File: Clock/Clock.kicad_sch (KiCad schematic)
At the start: 65 parts, among them J1 Conn buss, J10 Conn_buss, J11 Conn_buss, J12 Conn_buss, J13 Register_A-1,2 LED Conn, J14 Register_B-1,2 LED Conn, J15 Program Counter LED Conn, J16 Memory Address Reg LED Conn, J17 Instruction Reg LED Conn, J18 Conn_01x02_Pin, J19 Conn_02x04_Top_Bottom, J2 USB4125-GF-A, J3 Fuse-Block, J4 Conn buss, J5 Conn_buss, J6 Conn_buss, J7 Conn_buss, J8 Conn_buss, J9 Conn_buss, SW1 SW_CLK_mono, SW2 SW_Select_Mon/Ast, SW3 SW_SPST, SW4 SW_Select_Oscilator, U1 NE555P, U10 CD74HCT153E, U2 NE555P, U3 NE555P, U4 74LS04, U5 74LS08, U6 CD74HCT14E, U7 NE555P, U9 74HCT244, Y1 ECS-100AX-010

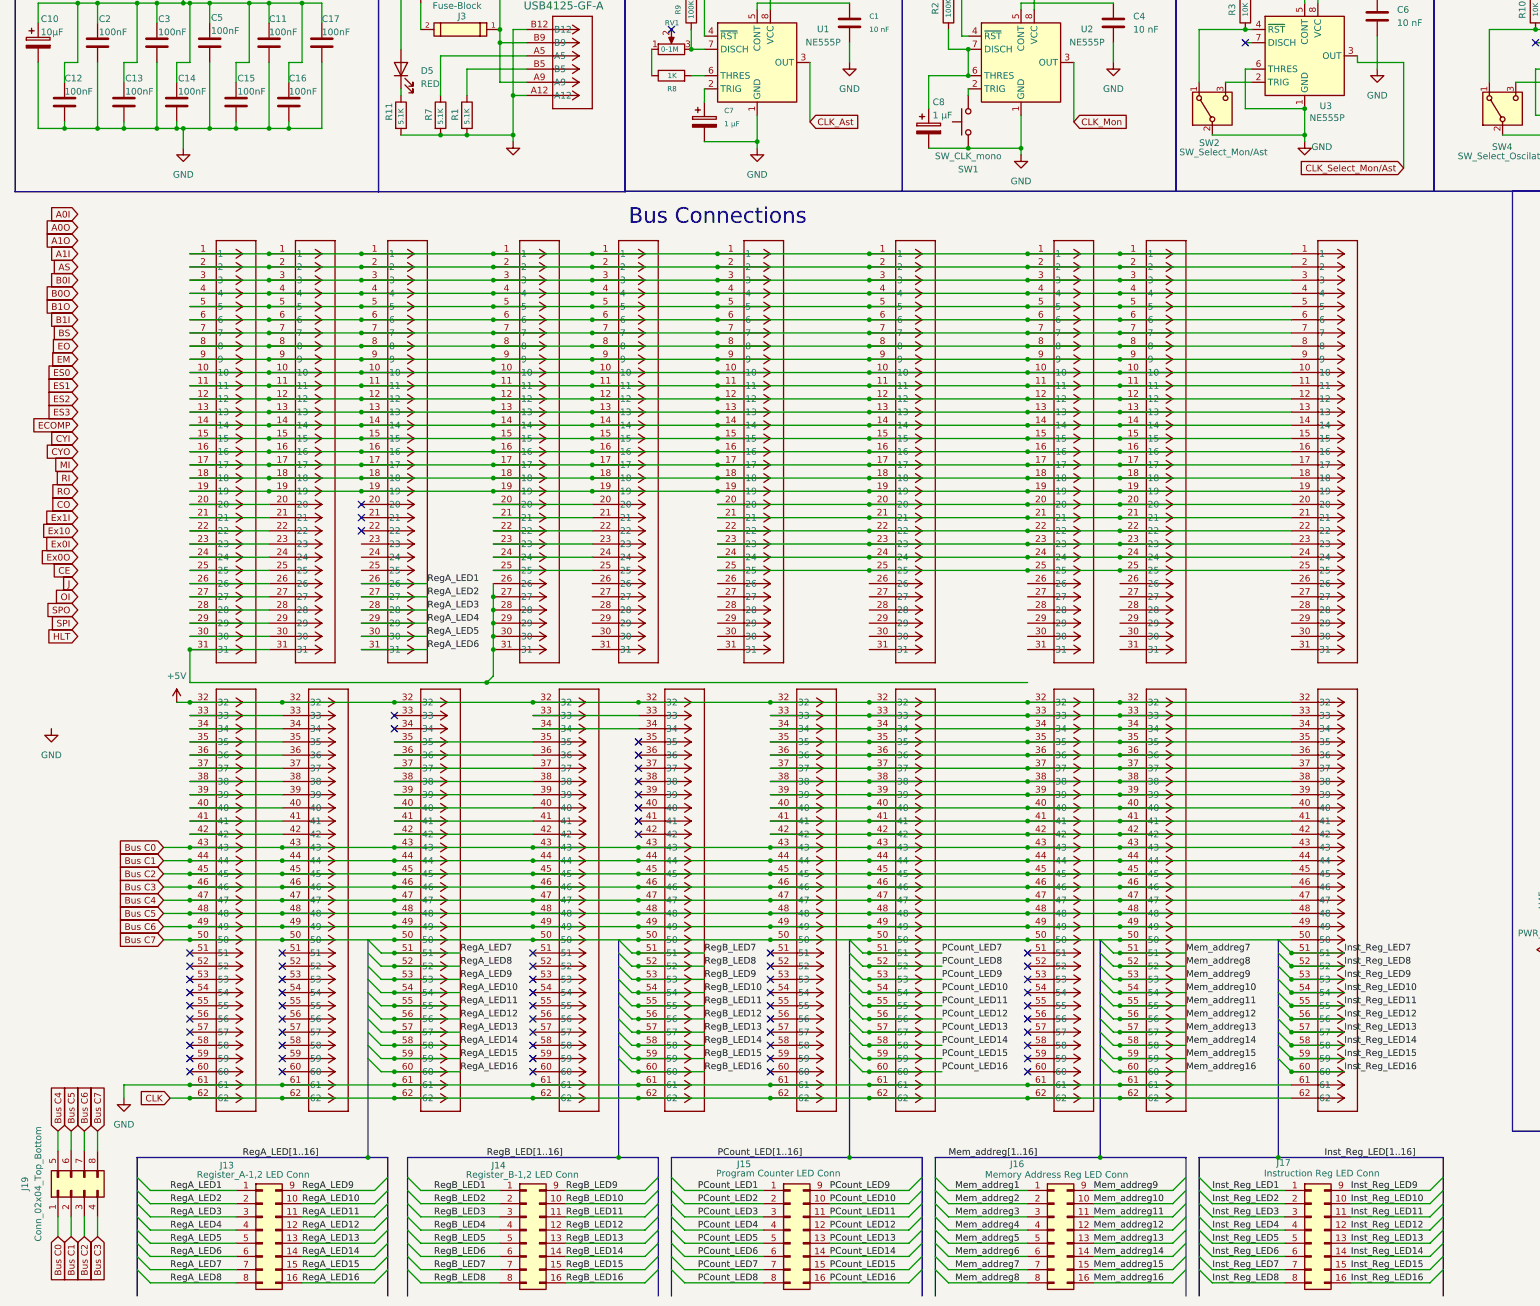
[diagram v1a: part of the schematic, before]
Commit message: Routed bus connector
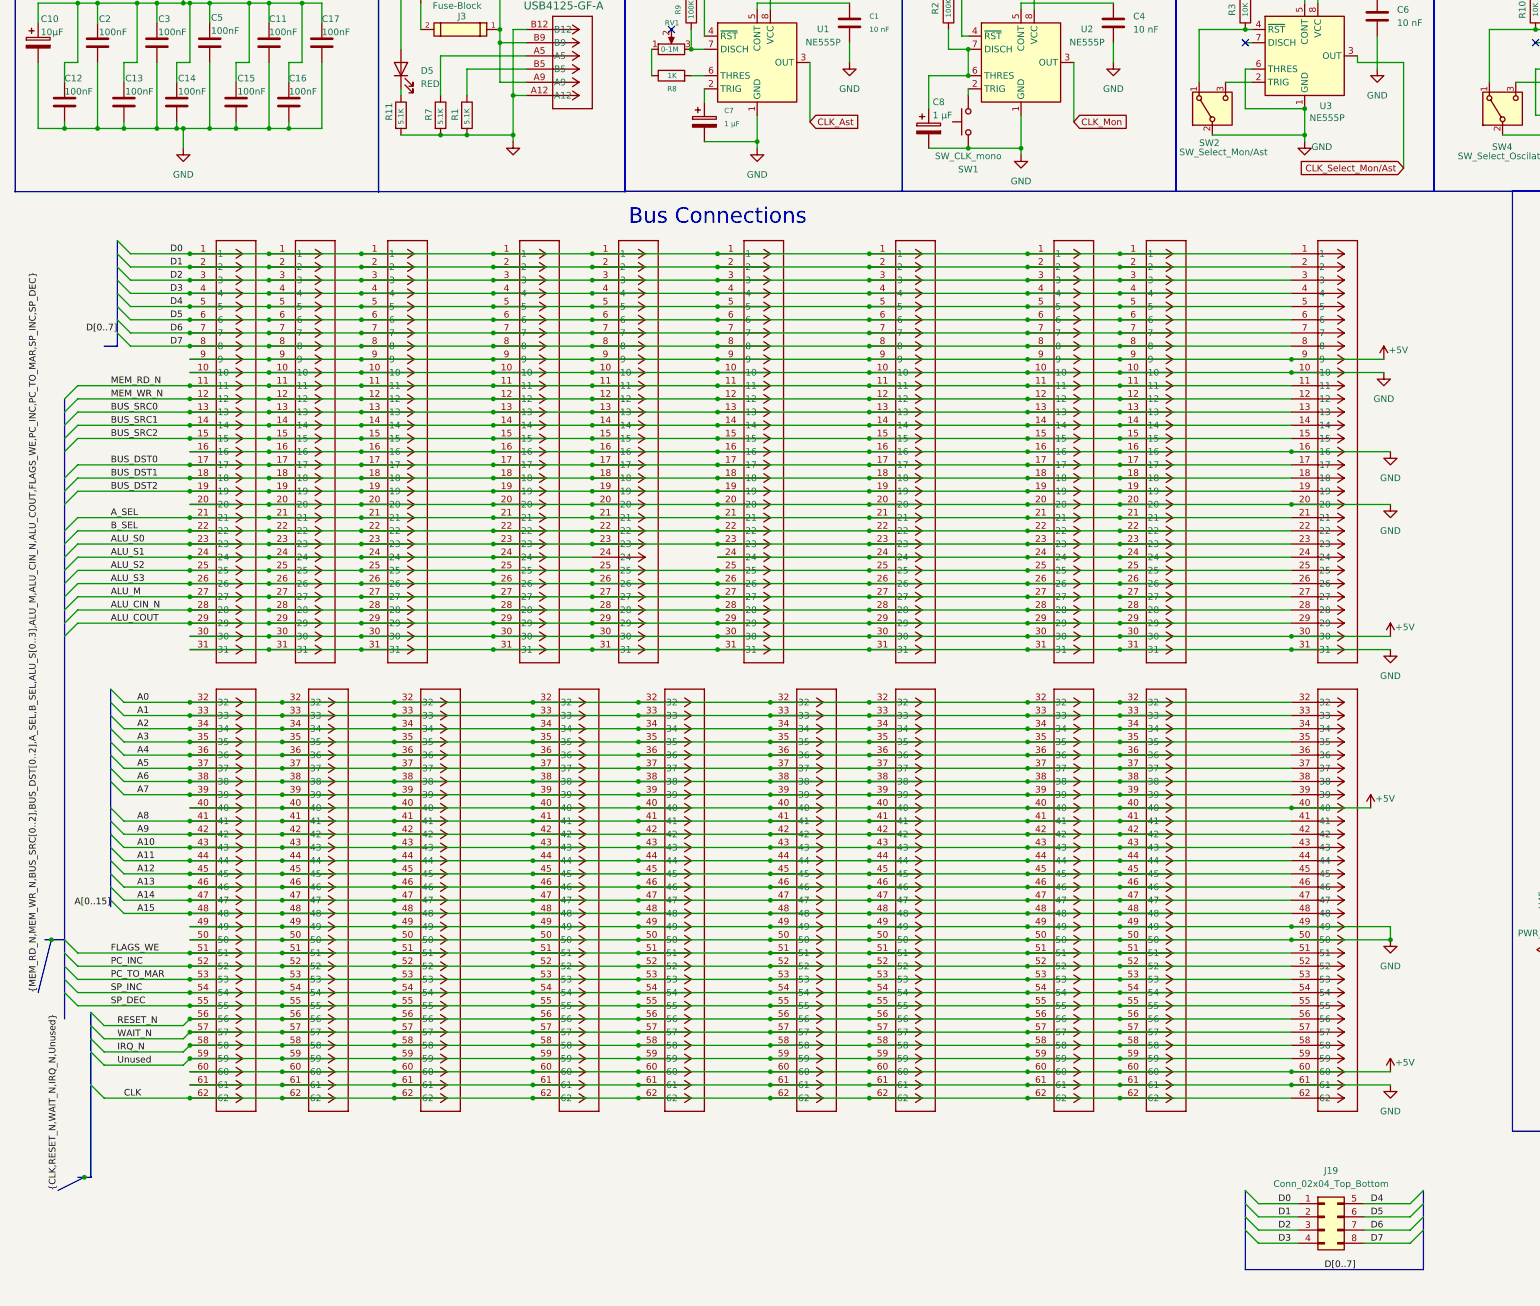
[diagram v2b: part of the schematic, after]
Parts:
- removed J13: Register_A-1,2 LED Conn, Connector_PinHeader_2.54mm:PinHeader_2x08_P2.54mm_Vertical, symbol Connector_Generic:Conn_02x08_Top_Bottom
- removed J14: Register_B-1,2 LED Conn, Connector_PinHeader_2.54mm:PinHeader_2x08_P2.54mm_Vertical, symbol Connector_Generic:Conn_02x08_Top_Bottom
- removed J15: Program Counter LED Conn, Connector_PinHeader_2.54mm:PinHeader_2x08_P2.54mm_Vertical, symbol Connector_Generic:Conn_02x08_Top_Bottom
- removed J16: Memory Address Reg LED Conn, Connector_PinHeader_2.54mm:PinHeader_2x08_P2.54mm_Vertical, symbol Connector_Generic:Conn_02x08_Top_Bottom
- removed J17: Instruction Reg LED Conn, Connector_PinHeader_2.54mm:PinHeader_2x08_P2.54mm_Vertical, symbol Connector_Generic:Conn_02x08_Top_Bottom
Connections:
- net Inst_Reg_LED10 is gone; now on net SP_INC: J1.54
- net Inst_Reg_LED11 is gone; now on net SP_DEC: J1.55
- net Inst_Reg_LED12 is gone; now on net RESET_N: J1.56
- net Inst_Reg_LED13 is gone; now on net WAIT_N: J1.57
- net Inst_Reg_LED14 is gone; now on net IRQ_N: J1.58
- net Inst_Reg_LED15 is gone; now on net Unused: J1.59
- net Inst_Reg_LED16 is gone; now on net +5V: J1.60
- net Inst_Reg_LED7 is gone; now on net FLAGS_WE: J1.51
- net Inst_Reg_LED8 is gone; now on net PC_INC: J1.52
- net Inst_Reg_LED9 is gone; now on net PC_TO_MAR: J1.53
- net Mem_addreg10 is gone; now on net SP_INC: J5.54
- net Mem_addreg11 is gone; now on net SP_DEC: J5.55
- net Mem_addreg12 is gone; now on net RESET_N: J5.56
- net Mem_addreg13 is gone; now on net WAIT_N: J5.57
- net Mem_addreg14 is gone; now on net IRQ_N: J5.58
- net Mem_addreg15 is gone; now on net Unused: J5.59
- net Mem_addreg16 is gone; now on net +5V: J5.60
- net Mem_addreg7 is gone; now on net FLAGS_WE: J5.51
- net Mem_addreg8 is gone; now on net PC_INC: J5.52
- net Mem_addreg9 is gone; now on net PC_TO_MAR: J5.53
- net PCount_LED10 is gone; now on net SP_INC: J8.54
- net PCount_LED11 is gone; now on net SP_DEC: J8.55
- net PCount_LED12 is gone; now on net RESET_N: J8.56
- net PCount_LED13 is gone; now on net WAIT_N: J8.57
- net PCount_LED14 is gone; now on net IRQ_N: J8.58
- net PCount_LED15 is gone; now on net Unused: J8.59
- net PCount_LED16 is gone; now on net +5V: J8.60
- net PCount_LED7 is gone; now on net FLAGS_WE: J8.51
- net PCount_LED8 is gone; now on net PC_INC: J8.52
- net PCount_LED9 is gone; now on net PC_TO_MAR: J8.53
- net RegA_LED1 is gone; now on net ALU_S3: J11.26
- net RegA_LED10 is gone; now on net SP_INC: J11.54
- net RegA_LED11 is gone; now on net SP_DEC: J11.55
- net RegA_LED12 is gone; now on net RESET_N: J11.56
- net RegA_LED13 is gone; now on net WAIT_N: J11.57
- net RegA_LED14 is gone; now on net IRQ_N: J11.58
- net RegA_LED15 is gone; now on net Unused: J11.59
- net RegA_LED16 is gone; now on net +5V: J11.60
- net RegA_LED2 is gone; now on net ALU_M: J11.27
- net RegA_LED3 is gone; now on net ALU_CIN_N: J11.28
- net RegA_LED4 is gone; now on net ALU_COUT: J11.29
- net RegA_LED5 is gone; now on net +5V: J11.30
- net RegA_LED6 is gone; now on net GND: J11.31
- net RegA_LED7 is gone; now on net FLAGS_WE: J11.51
- net RegA_LED8 is gone; now on net PC_INC: J11.52
- net RegA_LED9 is gone; now on net PC_TO_MAR: J11.53
- net RegB_LED10 is gone; now on net SP_INC: J9.54
- net RegB_LED11 is gone; now on net SP_DEC: J9.55
- net RegB_LED12 is gone; now on net RESET_N: J9.56
- net RegB_LED13 is gone; now on net WAIT_N: J9.57
- net RegB_LED14 is gone; now on net IRQ_N: J9.58
- net RegB_LED15 is gone; now on net Unused: J9.59
- net RegB_LED16 is gone; now on net +5V: J9.60
- net RegB_LED7 is gone; now on net FLAGS_WE: J9.51
- net RegB_LED8 is gone; now on net PC_INC: J9.52
- net RegB_LED9 is gone; now on net PC_TO_MAR: J9.53
- net +5V: now also J1.30, J1.40, J1.9, J10.30, J10.40, J10.60, J10.9, J11.40, J11.9, J12.30, J12.40, J12.60, J12.9, J4.30, J4.40, J4.60, J4.9, J5.30, J5.40, J5.9, J6.30, J6.40, J6.60, J6.9, J7.30, J7.40, J7.60, J7.9, J8.30, J8.40, J8.9, J9.30, J9.40, J9.9; no longer J1.32, J10.32, J11.32, J12.32, J4.32, J5.32, J6.32, J7.32, J8.32, J9.32
- net GND: now also J1.10, J1.16, J1.20, J1.31, J1.49, J1.50, J10.10, J10.16, J10.20, J10.31, J10.49, J10.50, J11.10, J11.16, J11.20, J11.49, J11.50, J12.10, J12.16, J12.20, J12.31, J12.49, J12.50, J4.10, J4.16, J4.20, J4.31, J4.49, J4.50, J5.10, J5.16, J5.20, J5.31, J5.49, J5.50, J6.10, J6.16, J6.20, J6.31, J6.49, J6.50, J7.10, J7.16, J7.20, J7.31, J7.49, J7.50, J8.10, J8.16, J8.20, J8.31, J8.49, J8.50, J9.10, J9.16, J9.20, J9.31, J9.49, J9.50
- net D0: now reaches J1.1, J10.1, J11.1, J12.1, J4.1, J5.1, J6.1, J7.1, J8.1, J9.1
- net D0: now also J19.1 (Pin_1)
- net MEM_RD_N: now reaches J1.11, J10.11, J11.11, J12.11, J4.11, J5.11, J6.11, J7.11, J8.11, J9.11
- net MEM_WR_N: now reaches J1.12, J10.12, J11.12, J12.12, J4.12, J5.12, J6.12, J7.12, J8.12, J9.12
- net BUS_SRC0: now reaches J1.13, J10.13, J11.13, J12.13, J4.13, J5.13, J6.13, J7.13, J8.13, J9.13
- net BUS_SRC1: now reaches J1.14, J10.14, J11.14, J12.14, J4.14, J5.14, J6.14, J7.14, J8.14, J9.14
- net BUS_SRC2: now reaches J1.15, J10.15, J11.15, J12.15, J4.15, J5.15, J6.15, J7.15, J8.15, J9.15
- net BUS_DST0: now reaches J1.17, J10.17, J11.17, J12.17, J4.17, J5.17, J6.17, J7.17, J8.17, J9.17
- net BUS_DST1: now reaches J1.18, J10.18, J11.18, J12.18, J4.18, J5.18, J6.18, J7.18, J8.18, J9.18
- net BUS_DST2: now reaches J1.19, J10.19, J11.19, J12.19, J4.19, J5.19, J6.19, J7.19, J8.19, J9.19
- net D1: now reaches J1.2, J10.2, J11.2, J12.2, J4.2, J5.2, J6.2, J7.2, J8.2, J9.2
- net D1: now also J19.2 (Pin_2)
- net A_SEL: now reaches J7.21, J9.21
- net A_SEL: now also J1.21, J10.21, J11.21, J12.21, J4.21, J5.21, J6.21, J8.21
- net B_SEL: now reaches J7.22, J9.22
- net B_SEL: now also J1.22, J10.22, J11.22, J12.22, J4.22, J5.22, J6.22, J8.22
- net ALU_S0: now reaches J7.23, J9.23
- net ALU_S0: now also J1.23, J10.23, J11.23, J12.23, J4.23, J5.23, J6.23, J8.23
- net ALU_S1: now reaches J7.24, J9.24
- net ALU_S1: now also J10.24, J11.24, J12.24
- net ALU_S2: now reaches J7.25, J9.25
- net ALU_S2: now also J1.25, J10.25, J11.25, J12.25, J4.25, J5.25, J6.25, J8.25
- net D2: now reaches J1.3, J10.3, J11.3, J12.3, J4.3, J5.3, J6.3, J7.3, J8.3, J9.3
- net D2: now also J19.3 (Pin_3)
- net D3: now reaches J1.4, J10.4, J11.4, J12.4, J4.4, J5.4, J6.4, J7.4, J8.4, J9.4
- net D3: now also J19.4 (Pin_4)
- net D4: now reaches J1.5, J10.5, J11.5, J12.5, J4.5, J5.5, J6.5, J7.5, J8.5, J9.5
- net D4: now also J19.5 (Pin_5)
- net D5: now reaches J1.6, J10.6, J11.6, J12.6, J4.6, J5.6, J6.6, J7.6, J8.6, J9.6
- net D5: now also J19.6 (Pin_6)
- net D6: now reaches J1.7, J10.7, J11.7, J12.7, J4.7, J5.7, J6.7, J7.7, J8.7, J9.7
- net D6: now also J19.7 (Pin_7)
- net D7: now reaches J1.8, J10.8, J11.8, J12.8, J4.8, J5.8, J6.8, J7.8, J8.8, J9.8
- net D7: now also J19.8 (Pin_8)
- net ALU_S3: now reaches J10.26, J12.26
- net ALU_S3: now also J1.26, J4.26, J5.26, J6.26, J7.26, J8.26, J9.26
- net ALU_M: now reaches J10.27, J12.27
- net ALU_M: now also J1.27, J4.27, J5.27, J6.27, J7.27, J8.27, J9.27
- net ALU_CIN_N: now reaches J10.28, J12.28
- net ALU_CIN_N: now also J1.28, J4.28, J5.28, J6.28, J7.28, J8.28, J9.28
- net ALU_COUT: now reaches J10.29, J12.29
- net ALU_COUT: now also J1.29, J4.29, J5.29, J6.29, J7.29, J8.29, J9.29
- net A1: now reaches J1.33, J4.33, J5.33, J6.33, J8.33
- net A1: now also J10.33, J11.33, J12.33, J7.33, J9.33
- net A2: now reaches J1.34, J4.34, J5.34, J6.34, J8.34
- net A2: now also J10.34, J11.34, J12.34, J7.34, J9.34
- net A3: now reaches J1.35, J4.35, J5.35, J6.35, J8.35
- net A3: now also J10.35, J11.35, J12.35, J7.35, J9.35
- net A4: now reaches J1.36, J4.36, J5.36, J6.36, J8.36
- net A4: now also J10.36, J11.36, J12.36, J7.36, J9.36
- net A5: now reaches J1.37, J4.37, J5.37, J6.37, J8.37
- net A5: now also J10.37, J11.37, J12.37, J7.37, J9.37
- net A6: now reaches J1.38, J4.38, J5.38, J6.38, J8.38
- net A6: now also J10.38, J11.38, J12.38, J7.38, J9.38
- net A7: now reaches J1.39, J4.39, J5.39, J6.39, J8.39
- net A7: now also J10.39, J11.39, J12.39, J7.39, J9.39
- net A8: now reaches J1.41, J4.41, J5.41, J6.41, J8.41
- net A8: now also J10.41, J11.41, J12.41, J7.41, J9.41
- net A9: now reaches J1.42, J4.42, J5.42, J6.42, J8.42
- net A9: now also J10.42, J11.42, J12.42, J7.42, J9.42
- net FLAGS_WE: now reaches J4.51
- net FLAGS_WE: now also J10.51, J12.51, J6.51, J7.51
- net PC_INC: now reaches J4.52
- net PC_INC: now also J10.52, J12.52, J6.52, J7.52
- net PC_TO_MAR: now reaches J4.53
- net PC_TO_MAR: now also J10.53, J12.53, J6.53, J7.53
- net SP_INC: now reaches J4.54
- net SP_INC: now also J10.54, J12.54, J6.54, J7.54
- net SP_DEC: now reaches J4.55
- net SP_DEC: now also J10.55, J12.55, J6.55, J7.55
- net RESET_N: now reaches J4.56
- net RESET_N: now also J10.56, J12.56, J6.56, J7.56
- net WAIT_N: now reaches J4.57
- net WAIT_N: now also J10.57, J12.57, J6.57, J7.57
- net IRQ_N: now reaches J4.58
- net IRQ_N: now also J10.58, J12.58, J6.58, J7.58
- net Unused: now reaches J4.59
- net Unused: now also J10.59, J12.59, J6.59, J7.59
- net Bus C0 renamed A10
- net A10: no longer J19.1 (Pin_1)
- net Bus C1 renamed A11
- net A11: no longer J19.2 (Pin_2)
- net Bus C2 renamed A12
- net A12: no longer J19.3 (Pin_3)
- net Bus C3 renamed A13
- net A13: no longer J19.4 (Pin_4)
- net Bus C4 renamed A14
- net A14: no longer J19.5 (Pin_5)
- net Bus C5 renamed A15
- net A15: no longer J19.6 (Pin_6)
- removed net Bus C6: J1.49, J10.49, J11.49, J12.49, J19.7 (Pin_7), J4.49, J5.49, J6.49, J7.49, J8.49, J9.49
- removed net Bus C7: J1.50, J10.50, J11.50, J12.50, J19.8 (Pin_8), J4.50, J5.50, J6.50, J7.50, J8.50, J9.50
- new net A0: J1.32, J10.32, J11.32, J12.32, J4.32, J5.32, J6.32, J7.32, J8.32, J9.32
- no-connect marks 87 -> 24
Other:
- moved on the sheet: J19
